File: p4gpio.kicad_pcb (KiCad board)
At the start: 4 copper layers, 88.9 x 22.9 mm, 61 parts, among them J1 C2760486, J10 Conn_01x04_Socket, J2 C2760486, J3 Conn_01x08_Pin, J4 Conn_01x08_Pin, J5 Conn_01x08_Pin, J6 Conn_01x08_Pin, J7 Conn_01x08_Pin, J8 Conn_01x08_Pin, J9 Conn_01x04_Socket, U1 TLV62569DBV, U3 W25Q128JVS, Y1 40MHz(+-10 ppm) C501798

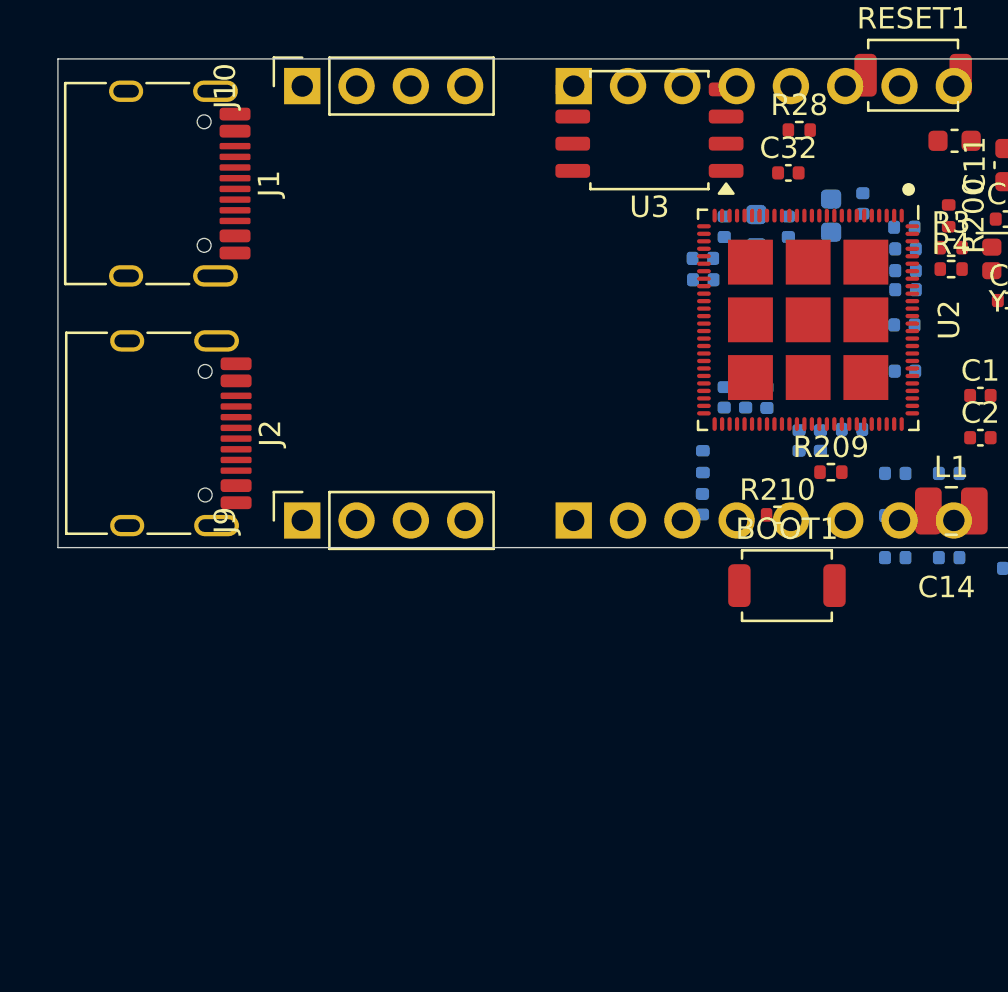
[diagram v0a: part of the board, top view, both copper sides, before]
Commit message: Schematic done except for GPIO
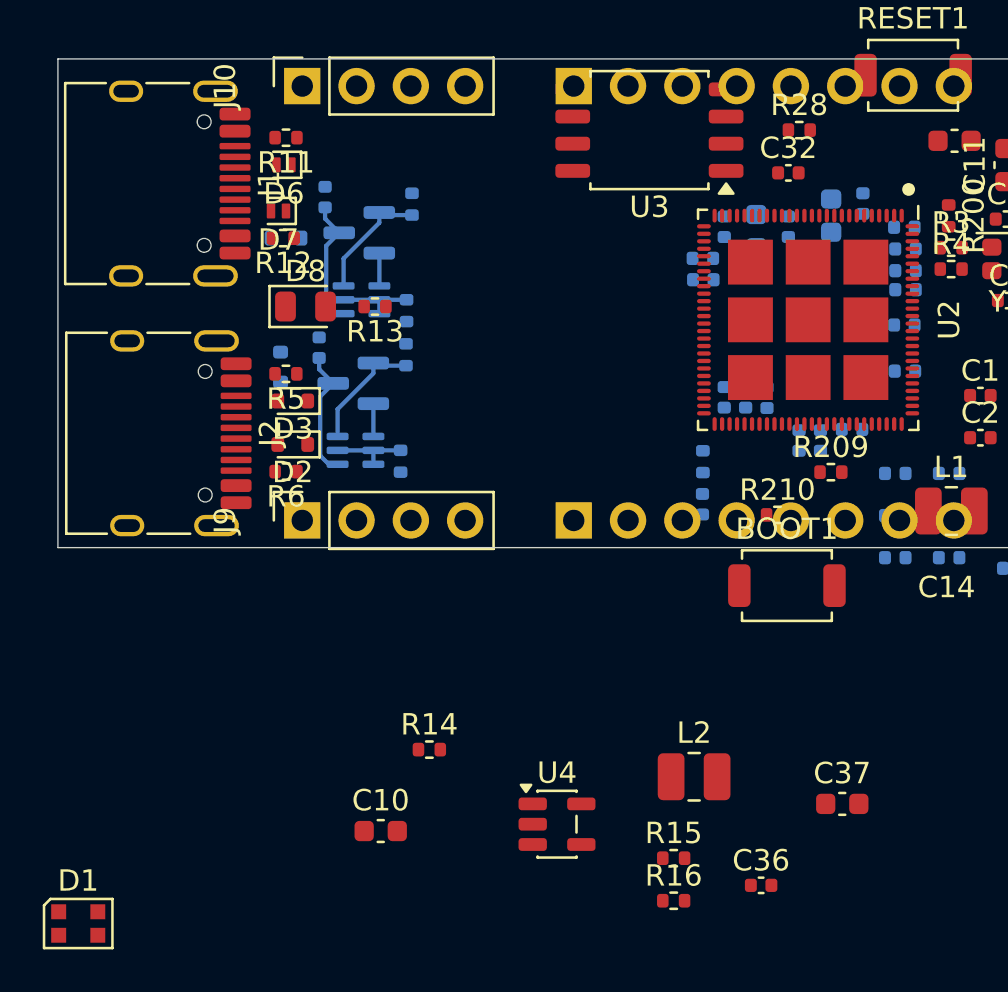
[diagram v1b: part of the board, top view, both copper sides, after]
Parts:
- added C10: 10uF, Capacitor_SMD:C_0603_1608Metric, F.Cu at (115.4, 126.3)
- added C34: 1uF/16V(10%), Capacitor_SMD:C_0402_1005Metric, B.Cu at (112.5, 103.7)
- added C35: 1uF/16V(10%), Capacitor_SMD:C_0402_1005Metric, B.Cu at (112.8, 96.6)
- added C36: 22pF, Capacitor_SMD:C_0402_1005Metric, F.Cu at (133.2, 128.8)
- added C37: 10uF, Capacitor_SMD:C_0603_1608Metric, F.Cu at (137.0, 125.0)
- added D1: WS2812B-2020, LED_SMD:LED_WS2812B-2020_PLCC4_2.0x2.0mm, F.Cu at (101.3, 130.6)
- added D2: LESD5D5.0CT1G, Diode_SMD:D_SOD-523, F.Cu at (111.3, 108.2)
- added D3: LESD5D5.0CT1G, Diode_SMD:D_SOD-523, F.Cu at (111.3, 106.2)
- added D4: LESD5D5.0CT1G, Diode_SMD:D_SOD-523, B.Cu at (110.7, 104.6)
- added D5: LESD5D5.0CT1G, Diode_SMD:D_SOD-523, B.Cu at (111.0, 98.6)
- added D6: ESD7951ST5G, Diode_SMD:D_SOD-882, F.Cu at (110.9, 95.1)
- added D7: ESD7951ST5G, Diode_SMD:D_SOD-882, F.Cu at (110.6, 97.3)
- added D8: GREEN LED, Diode_SMD:D_0805_2012Metric, F.Cu at (111.9, 101.8)
- added L2: 2.2uH, Inductor_SMD:L_1008_2520Metric, F.Cu at (130.1, 123.7)
- added Q1: MBT3906DW1, Package_TO_SOT_SMD:SOT-363_SC-70-6, B.Cu at (114.3, 108.5)
- added Q2: AO3401A, Package_TO_SOT_SMD:SOT-23, B.Cu at (114.1, 105.3)
- added Q3: MBT3906DW1, Package_TO_SOT_SMD:SOT-363_SC-70-6, B.Cu at (114.5, 101.4)
- added Q4: AO3401A, Package_TO_SOT_SMD:SOT-23, B.Cu at (114.4, 98.3)
- added R10: 51K(1%), Resistor_SMD:R_0402_1005Metric, B.Cu at (116.9, 97.0)
- added R11: 5.1K(1%), Resistor_SMD:R_0402_1005Metric, F.Cu at (111.0, 93.9)
- added R12: 5.1K(1%), Resistor_SMD:R_0402_1005Metric, F.Cu at (110.9, 98.6)
- added R13: 5.1K(1%), Resistor_SMD:R_0402_1005Metric, F.Cu at (115.2, 101.8)
- added R14: 10K, Resistor_SMD:R_0402_1005Metric, F.Cu at (117.7, 122.5)
- added R15: 100K(1%), Resistor_SMD:R_0402_1005Metric, F.Cu at (129.1, 127.6)
- added R16: 22.1K(1%), Resistor_SMD:R_0402_1005Metric, F.Cu at (129.1, 129.5)
- added R5: 5.1K(1%), Resistor_SMD:R_0402_1005Metric, F.Cu at (111.0, 104.9)
- added R6: 5.1K(1%), Resistor_SMD:R_0402_1005Metric, F.Cu at (111.0, 109.5)
- added R7: 10K(1%), Resistor_SMD:R_0402_1005Metric, B.Cu at (116.4, 109.0)
- added R8: 51K(1%), Resistor_SMD:R_0402_1005Metric, B.Cu at (116.6, 104.0)
- added R9: 10K(1%), Resistor_SMD:R_0402_1005Metric, B.Cu at (116.6, 101.9)
- added U4: TLV62569DBV, Package_TO_SOT_SMD:SOT-23-5, F.Cu at (123.7, 126.0)
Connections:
- net Net-(J1-VBUS-PadA4) renamed /HS_VBUS
- net Net-(J2-VBUS-PadA4) renamed /FS_VBUS
- J1 pad A5: unconnected-(J1-CC1-PadA5) -> Net-(J1-CC1)
- J1 pad A6: unconnected-(J1-D+-PadA6) -> /HS_DP
- J1 pad A7: unconnected-(J1-D--PadA7) -> /HS_DM
- J1 pad B5: unconnected-(J1-CC2-PadB5) -> Net-(J1-CC2)
- J1 pad B6: unconnected-(J1-D+-PadB6) -> /HS_DP
- J1 pad B7: unconnected-(J1-D--PadB7) -> /HS_DM
- J2 pad A5: unconnected-(J2-CC1-PadA5) -> Net-(J2-CC1)
- J2 pad A6: unconnected-(J2-D+-PadA6) -> /FS_DP
- J2 pad A7: unconnected-(J2-D--PadA7) -> /FS_DM
- J2 pad B5: unconnected-(J2-CC2-PadB5) -> Net-(J2-CC2)
- J2 pad B6: unconnected-(J2-D+-PadB6) -> /FS_DP
- J2 pad B7: unconnected-(J2-D--PadB7) -> /FS_DM
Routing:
- net /HS_VBUS: track 0.00 -> 6.08 mm
- net /FS_VBUS: track 0.00 -> 6.08 mm
- net Net-(Q1B-C2): track 0.00 -> 5.71 mm
- net Net-(Q3B-C2): track 0.00 -> 5.71 mm
- net Net-(Q1A-B1): track 0.00 -> 3.60 mm
- net Net-(Q3A-B1): track 0.00 -> 3.60 mm
- net VBUS: track 0.00 -> 3.07 mm

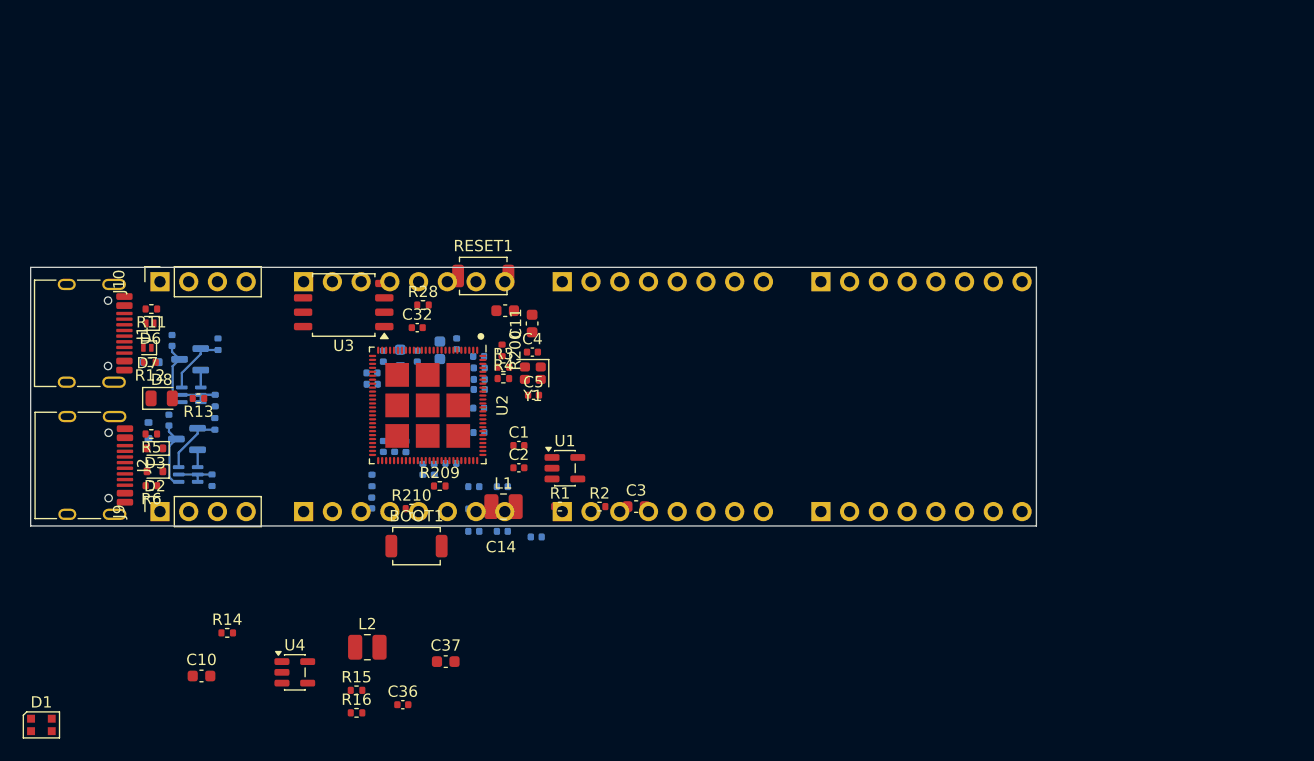
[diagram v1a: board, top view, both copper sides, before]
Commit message: Setup design rules. Start to match up pins
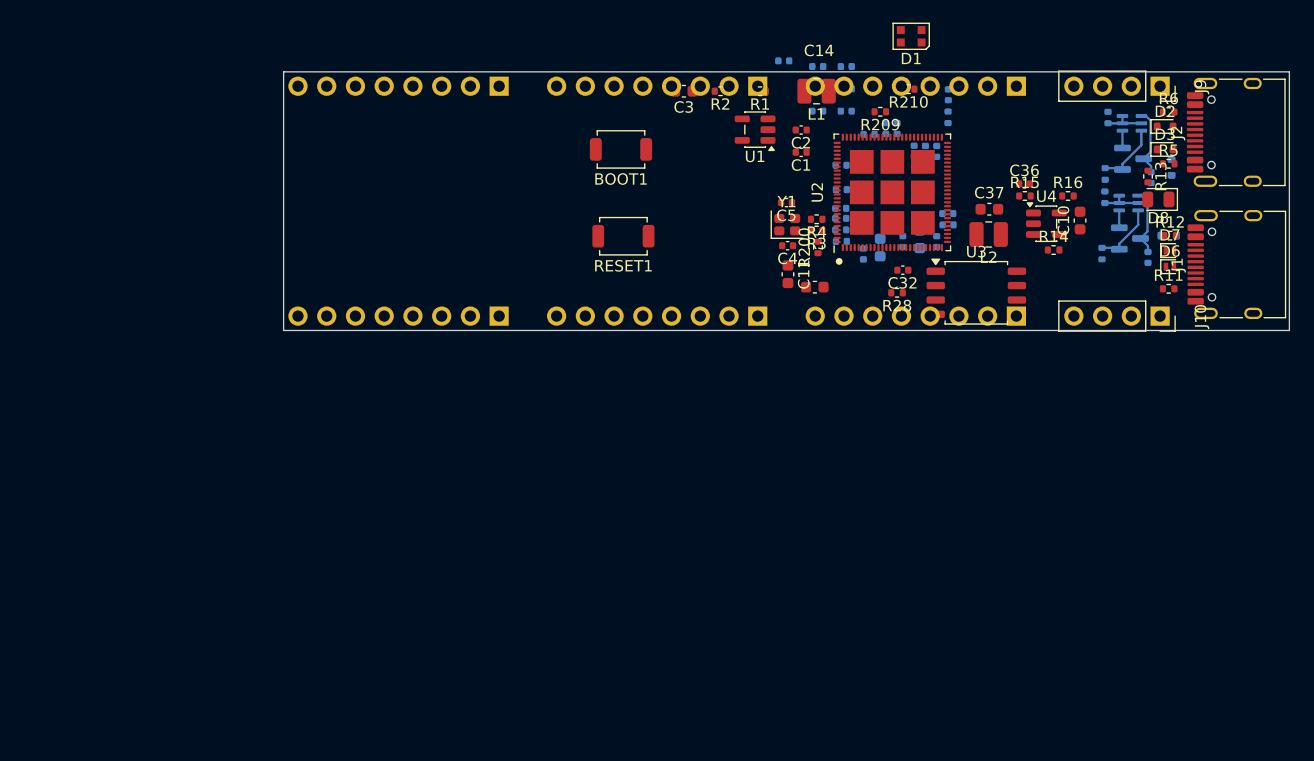
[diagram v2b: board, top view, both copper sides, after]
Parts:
- moved J2 106.8 mm to (207.3, 78.2), turned to 90 degrees
- moved J1 103.0 mm to (207.3, 89.9), turned to 90 degrees
- moved D1 98.1 mm to (178.2, 69.7), turned to 180 degrees
- moved J9 96.1 mm to (200.2, 74.2), turned to -90 degrees
- moved R6 95.8 mm to (200.9, 76.4), turned to 0 degrees
- moved D2 94.4 mm to (200.6, 77.7), turned to 0 degrees
- moved D4 93.4 mm to (201.2, 81.3), turned to 90 degrees
- moved D3 93.1 mm to (200.6, 79.7), turned to 0 degrees
- moved R5 93.0 mm to (200.9, 81.0), turned to 0 degrees
- moved R12 90.9 mm to (201.1, 87.4), turned to 0 degrees
- moved D7 90.8 mm to (201.0, 88.7), turned to 0 degrees
- moved D5 90.6 mm to (200.9, 87.4), turned to 0 degrees
- moved D6 90.3 mm to (201.0, 90.1), turned to 0 degrees
- moved R11 89.9 mm to (200.9, 92.1), turned to 0 degrees
- moved D8 89.8 mm to (200.0, 84.2), turned to 180 degrees
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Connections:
- D2 pad 2: /FS_DP -> /FS_D+
- D3 pad 2: /FS_DM -> /FS_D-
- D6 pad 2: /HS_DM -> /HS_D-
- D7 pad 2: /HS_DP -> /HS_D+
- J1 pad A6: /HS_DP -> /HS_D+
- J1 pad A7: /HS_DM -> /HS_D-
- J1 pad B6: /HS_DP -> /HS_D+
- J1 pad B7: /HS_DM -> /HS_D-
- J2 pad A6: /FS_DP -> /FS_D+
- J2 pad A7: /FS_DM -> /FS_D-
- J2 pad B6: /FS_DP -> /FS_D+
- J2 pad B7: /FS_DM -> /FS_D-
- J3 pad 1: unconnected-(J3-Pin_1-Pad1) -> /T3_7
- J3 pad 2: unconnected-(J3-Pin_2-Pad2) -> /T3_6
- J3 pad 3: unconnected-(J3-Pin_3-Pad3) -> /T3_5
- J3 pad 4: unconnected-(J3-Pin_4-Pad4) -> /T3_4
- J3 pad 5: unconnected-(J3-Pin_5-Pad5) -> /T3_3
- J3 pad 6: unconnected-(J3-Pin_6-Pad6) -> /T3_2
- J3 pad 7: unconnected-(J3-Pin_7-Pad7) -> /T3_1
- J3 pad 8: unconnected-(J3-Pin_8-Pad8) -> /T3_0
- J4 pad 1: unconnected-(J4-Pin_1-Pad1) -> /T2_7
- J4 pad 2: unconnected-(J4-Pin_2-Pad2) -> /T2_6
- J4 pad 3: unconnected-(J4-Pin_3-Pad3) -> /T2_5
- J4 pad 4: unconnected-(J4-Pin_4-Pad4) -> /T2_4
- J4 pad 5: unconnected-(J4-Pin_5-Pad5) -> /T2_3
- J4 pad 6: unconnected-(J4-Pin_6-Pad6) -> /T2_2
- J4 pad 7: unconnected-(J4-Pin_7-Pad7) -> /T2_1
- J4 pad 8: unconnected-(J4-Pin_8-Pad8) -> /T2_0
- J5 pad 1: unconnected-(J5-Pin_1-Pad1) -> /T1_7
- J5 pad 2: unconnected-(J5-Pin_2-Pad2) -> /T1_6
- J5 pad 3: unconnected-(J5-Pin_3-Pad3) -> /T1_5
- J5 pad 4: unconnected-(J5-Pin_4-Pad4) -> /T1_4
- J5 pad 5: unconnected-(J5-Pin_5-Pad5) -> /T1_3
- J5 pad 6: unconnected-(J5-Pin_6-Pad6) -> /T1_2
- J5 pad 7: unconnected-(J5-Pin_7-Pad7) -> /T1_1
- J5 pad 8: unconnected-(J5-Pin_8-Pad8) -> /T1_0
- J6 pad 1: unconnected-(J6-Pin_1-Pad1) -> /B3_7
- J6 pad 2: unconnected-(J6-Pin_2-Pad2) -> /B3_6
- J6 pad 3: unconnected-(J6-Pin_3-Pad3) -> /B3_5
- J6 pad 4: unconnected-(J6-Pin_4-Pad4) -> /B3_4
- J6 pad 5: unconnected-(J6-Pin_5-Pad5) -> /B3_3
- J6 pad 6: unconnected-(J6-Pin_6-Pad6) -> /B3_2
- J6 pad 7: unconnected-(J6-Pin_7-Pad7) -> /B3_1
- J6 pad 8: unconnected-(J6-Pin_8-Pad8) -> /B3_0
- J7 pad 1: unconnected-(J7-Pin_1-Pad1) -> /B2_7
- J7 pad 2: unconnected-(J7-Pin_2-Pad2) -> /B2_6
- J7 pad 3: unconnected-(J7-Pin_3-Pad3) -> /B2_5
- J7 pad 4: unconnected-(J7-Pin_4-Pad4) -> /B2_4
- J7 pad 5: unconnected-(J7-Pin_5-Pad5) -> /B2_3
- J7 pad 6: unconnected-(J7-Pin_6-Pad6) -> /B2_2
- J7 pad 7: unconnected-(J7-Pin_7-Pad7) -> /B2_1
- J7 pad 8: unconnected-(J7-Pin_8-Pad8) -> /B2_0
- J8 pad 1: unconnected-(J8-Pin_1-Pad1) -> /B1_7
- J8 pad 2: unconnected-(J8-Pin_2-Pad2) -> /B1_6
- J8 pad 3: unconnected-(J8-Pin_3-Pad3) -> /B1_5
- J8 pad 4: unconnected-(J8-Pin_4-Pad4) -> /B1_4
- J8 pad 5: unconnected-(J8-Pin_5-Pad5) -> /B1_3
- J8 pad 6: unconnected-(J8-Pin_6-Pad6) -> /B1_2
- J8 pad 7: unconnected-(J8-Pin_7-Pad7) -> /B1_1
- J8 pad 8: unconnected-(J8-Pin_8-Pad8) -> /B1_0
- U2 pad 49: /Minimal P4 V3/HS_USB_DM -> /HS_D-
- U2 pad 50: /Minimal P4 V3/HS_USB_DP -> /HS_D+
- U2 pad 52: /Minimal P4 V3/GPIO24/ADC/USB_JTAG_DM -> /FS_D-
- U2 pad 53: /Minimal P4 V3/GPIO25/ADC/USB_JTAG_DP -> /FS_D+
- U2 pad 55: /Minimal P4 V3/GPIO26/ADC/USB -> /T3_7
- U2 pad 56: /Minimal P4 V3/GPIO27/ADC/USB -> /T3_6
- U2 pad 57: /Minimal P4 V3/GPIO28 -> /T3_5
- U2 pad 58: /Minimal P4 V3/GPIO29 -> /T3_4
- U2 pad 60: /Minimal P4 V3/GPIO30 -> /T3_3
- U2 pad 61: /Minimal P4 V3/GPIO31 -> /T3_2
- U2 pad 63: /Minimal P4 V3/GPIO32 -> /T3_1
- U2 pad 64: /Minimal P4 V3/GPIO33 -> /T3_0
- U2 pad 68: /Minimal P4 V3/GPIO36/BOOTMODE -> /T2_7
- U2 pad 69: /Minimal P4 V3/GPIO37/UART0_TXD -> /T2_6
- U2 pad 70: /Minimal P4 V3/GPIO38/UART0_RXD -> /T2_5
- U2 pad 80: /Minimal P4 V3/GPIO39 -> /T2_4
- U2 pad 81: /Minimal P4 V3/GPIO40 -> /T2_3
- U2 pad 82: /Minimal P4 V3/GPIO41 -> /T2_2
- U2 pad 83: /Minimal P4 V3/GPIO42 -> /T2_1
- U2 pad 84: /Minimal P4 V3/GPIO43 -> /T2_0

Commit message: Lots more routing and placement
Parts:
- removed C19, C22: 1uF, Capacitor_SMD:C_0402_1005Metric
- C11, C14, C2, C32, C36, R1, R14, R15, R16, R2, R200, R28: moved to B.Cu
- C15, C17: moved to F.Cu
- U3: footprint Package_SO:SOIC-8_5.3x5.3mm_P1.27mm -> Package_SON:WSON-8-1EP_6x5mm_P1.27mm_EP3.4x4.3mm
- moved D1 54.0 mm to (126.1, 84.2)
- moved RESET1 26.3 mm to (126.4, 88.3)
- moved BOOT1 26.2 mm to (126.3, 79.1)
- moved C3 12.3 mm to (169.2, 79.7), turned to -90 degrees
- moved R2 9.62 mm to (165.2, 83.4)
- moved C16 9.23 mm to (172.6, 81.2)
- moved L2 9.01 mm to (193.9, 86.2), turned to -90 degrees
- moved C14 8.86 mm to (172.6, 83.6), turned to 0 degrees
- moved R1 7.73 mm to (165.2, 82.3), turned to 0 degrees
- moved R14 7.70 mm to (194.1, 81.7), turned to 90 degrees
- moved C10 7.02 mm to (192.9, 79.0), turned to 180 degrees
- moved R28 6.68 mm to (183.3, 90.6), turned to 90 degrees
- moved C37 6.68 mm to (191.7, 85.8), turned to 90 degrees
- moved C13 6.49 mm to (172.6, 82.2)
- moved C32 6.39 mm to (181.9, 85.8)
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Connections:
- C30 pad 1: /Minimal P4 V3/VDDO_FLASH -> /Minimal P4 V3/VDD_FLASH
- C31 pad 1: /Minimal P4 V3/VDDO_FLASH -> /Minimal P4 V3/VDD_FLASH
- C32 pad 1: /Minimal P4 V3/VDDO_FLASH -> /Minimal P4 V3/VDD_FLASH
- C8 pad 1: +3.3V -> /Minimal P4 V3/VDD_HP
- R28 pad 2: /Minimal P4 V3/VDDO_FLASH -> /Minimal P4 V3/VDD_FLASH
- U2 pad 1: /Minimal P4 V3/GPIO1/ADC -> /B1_1
- U2 pad 10: /Minimal P4 V3/GPIO9/ADC -> /B2_1
- U2 pad 104: /Minimal P4 V3/GPIO0/ADC -> /B1_0
- U2 pad 11: /Minimal P4 V3/GPIO10/ADC -> /B2_2
- U2 pad 12: /Minimal P4 V3/GPIO11/ADC -> /B2_3
- U2 pad 13: /Minimal P4 V3/GPIO12/ADC -> /B2_4
- U2 pad 14: /Minimal P4 V3/GPIO13/ADC -> /B2_5
- U2 pad 15: /Minimal P4 V3/GPIO14/ADC -> /B2_6
- U2 pad 16: /Minimal P4 V3/GPIO15/ADC -> /B2_7
- U2 pad 17: /Minimal P4 V3/GPIO16/ADC -> /B3_0
- U2 pad 18: /Minimal P4 V3/GPIO17/ADC -> /B3_1
- U2 pad 19: /Minimal P4 V3/GPIO18/ADC -> /B3_2
- U2 pad 2: /Minimal P4 V3/GPIO2/ADC -> /B1_2
- U2 pad 20: /Minimal P4 V3/GPIO19/ADC -> /B3_3
- U2 pad 22: /Minimal P4 V3/GPIO20/ADC -> /B3_4
- U2 pad 23: /Minimal P4 V3/GPIO21/ADC -> /B3_5
- U2 pad 24: /Minimal P4 V3/GPIO22/ADC -> /B3_6
- U2 pad 25: /Minimal P4 V3/GPIO23/ADC -> /B3_7
- U2 pad 3: /Minimal P4 V3/GPIO3/ADC -> /B1_3
- U2 pad 30: /Minimal P4 V3/VDDO_FLASH -> /Minimal P4 V3/VDD_FLASH
- U2 pad 4: /Minimal P4 V3/GPIO4/ADC -> /B1_4
- U2 pad 5: /Minimal P4 V3/GPIO5/ADC -> /B1_5
- U2 pad 6: /Minimal P4 V3/GPIO6/ADC -> /B1_6
- U2 pad 7: /Minimal P4 V3/GPIO7/ADC -> /B1_7
- U2 pad 73: /Minimal P4 V3/VDDO_3 -> unconnected-(U2-VDDO_3-Pad73)
- U2 pad 74: /Minimal P4 V3/VDDO_4 -> unconnected-(U2-VDDO_4-Pad74)
- U2 pad 8: /Minimal P4 V3/GPIO8/ADC -> /B2_0
- U2 pad 86: /Minimal P4 V3/GPIO44 -> /T1_7
- U2 pad 87: /Minimal P4 V3/GPIO45 -> /T1_6
- U2 pad 88: /Minimal P4 V3/GPIO46 -> /T1_5
- U2 pad 89: /Minimal P4 V3/GPIO47 -> /T1_4
- U2 pad 90: /Minimal P4 V3/GPIO48 -> /T1_3
- U2 pad 91: +3.3V -> /Minimal P4 V3/VDD_HP
- U2 pad 92: /Minimal P4 V3/GPIO49/ADC -> /T1_2
- U2 pad 93: /Minimal P4 V3/GPIO50/ADC -> /T1_1
- U2 pad 94: /Minimal P4 V3/GPIO51/ADC -> /T1_0
- U3 pad 8: /Minimal P4 V3/VDDO_FLASH -> /Minimal P4 V3/VDD_FLASH
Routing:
- net +3.3V: track 0.00 -> 53.6 mm, vias 0 -> 9
- net /Minimal P4 V3/VDDO_PSRAM: track 0.00 -> 11.9 mm, vias 0 -> 3
- net /Minimal P4 V3/VDD_FLASH: track 0.00 -> 9.81 mm, vias 0 -> 1
- net /Minimal P4 V3/FLASH_D: track 0.00 -> 9.24 mm
- net /Minimal P4 V3/FLASH_CK: track 0.00 -> 8.05 mm
- net /Minimal P4 V3/FLASH_Q: track 0.00 -> 7.46 mm
- net /Minimal P4 V3/FLASH_WP: track 0.00 -> 6.84 mm
- net /Minimal P4 V3/FLASH_HOLD: track 0.00 -> 6.64 mm
- net /Minimal P4 V3/FLASH_CS: track 0.00 -> 5.26 mm, vias 0 -> 2
- net Net-(C5-Pad1): track 0.00 -> 4.29 mm
- net Net-(U2-XTAL_P): track 0.00 -> 3.36 mm
- net Net-(U2-XTAL_N): track 0.00 -> 3.10 mm
- net Net-(C4-Pad2): track 0.00 -> 3.06 mm
- net Net-(U2-VDD_HP_1): track 0.00 -> 2.26 mm, vias 0 -> 1
- net /Minimal P4 V3/VDD_HP: track 0.00 -> 1.97 mm, vias 0 -> 1
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- added copper zone on B.Cu, net GND
- added copper zone on F.Cu, net GND
- added copper zone on In1.Cu, net GND

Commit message: More power routing
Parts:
- moved R2 2.30 mm to (163.6, 81.8), turned to -90 degrees
- moved R14 2.29 mm to (192.6, 83.5), turned to 0 degrees
- moved R13 1.64 mm to (197.5, 82.0)
- moved R5 1.18 mm to (199.7, 80.9)
- moved R11 1.13 mm to (199.9, 91.5)
- moved R6 1.12 mm to (199.8, 76.5)
- moved R12 1.10 mm to (199.9, 87.4)
- moved D2 0.71 mm to (199.9, 77.8)
- moved D3 0.70 mm to (199.9, 79.7)
- moved D6 0.21 mm to (201.0, 90.3)
- moved D7 0.15 mm to (201.0, 88.5)
- moved R15 0.05 mm to (193.0, 81.9)
- turned R16 to 180 degrees
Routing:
- net +3.3V: track 53.6 -> 111.1 mm, vias 9 -> 14
- net /Minimal P4 V3/VDD_HP: track 1.97 -> 54.4 mm, vias 1 -> 9
- net /HS_D+: track 0.00 -> 32.3 mm
- net /HS_D-: track 0.00 -> 32.0 mm, vias 0 -> 2
- net /FS_D+: track 0.00 -> 28.1 mm
- net /FS_D-: track 0.00 -> 27.2 mm, vias 0 -> 2
- net VBUS: track 3.07 -> 27.8 mm, vias 0 -> 4
- net /Minimal P4 V3/FB_DCDC: track 0.00 -> 17.1 mm, vias 0 -> 2
- net /FS_VBUS: track 6.08 -> 20.2 mm, vias 0 -> 4
- net /HS_VBUS: track 6.08 -> 20.1 mm, vias 0 -> 4
- net Net-(U4-FB): track 0.00 -> 7.10 mm, vias 0 -> 1
- net GND: track 0.00 -> 4.77 mm, vias 38 -> 81
- net /Minimal P4 V3/EN_DCDC: track 0.00 -> 4.60 mm
- net Net-(J2-CC1): track 0.00 -> 3.59 mm
- net Net-(U1-SW): track 0.00 -> 3.50 mm
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
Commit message: more routing
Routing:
- net /B1_0: track 0.00 -> 49.8 mm
- net /B1_1: track 0.00 -> 47.4 mm
- net /B1_2: track 0.00 -> 45.4 mm
- net /B1_3: track 0.00 -> 43.3 mm
- net /B1_4: track 0.00 -> 41.2 mm
- net /B1_5: track 0.00 -> 39.1 mm
- net /B1_6: track 0.00 -> 37.0 mm
- net /B1_7: track 0.00 -> 35.4 mm
- net /B2_0: track 0.00 -> 30.3 mm, vias 0 -> 1
- net /B2_1: track 0.00 -> 28.4 mm, vias 0 -> 1
- net /B2_2: track 0.00 -> 26.4 mm, vias 0 -> 1
- net /B2_3: track 0.00 -> 24.5 mm, vias 0 -> 1
- net /RESET: track 2.75 -> 26.7 mm, vias 1 -> 2
- net /B2_4: track 0.00 -> 22.4 mm, vias 0 -> 1
- net /B2_5: track 0.00 -> 20.1 mm, vias 0 -> 1
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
